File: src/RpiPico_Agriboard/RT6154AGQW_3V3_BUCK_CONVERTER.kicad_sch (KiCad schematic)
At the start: 14 parts, among them U1 RT6154A/B

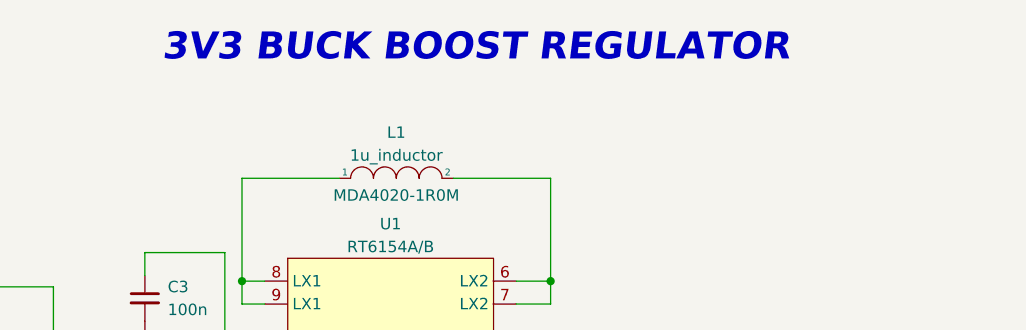
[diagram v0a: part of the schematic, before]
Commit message: Revert "schematic updates completed"
This reverts commit 0124993096667d53f20fd59dec80d3f5a1efcd43.
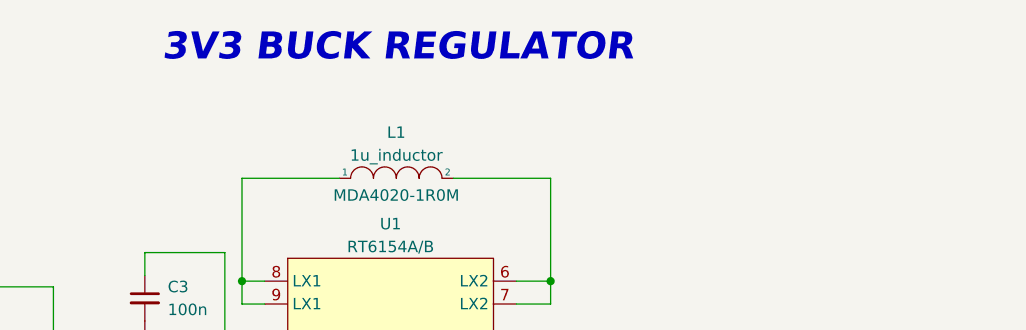
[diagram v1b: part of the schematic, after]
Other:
- note added: "3V3 BUCK REGULATOR"
- note removed: "3V3 BUCK BOOST REGULATOR"
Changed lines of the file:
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@@
     (stroke (width 0) (type default))
   )
-  (text "3V3 BUCK BOOST REGULATOR" (at 137.16 50.8 0)
+  (text "3V3 BUCK REGULATOR" (at 137.16 50.8 0)
     (effects (font (size 3 3) bold italic) (justify left bottom))
   )

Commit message: schematic updates completed
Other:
- note added: "3V3 BUCK BOOST REGULATOR"
- note removed: "3V3 BUCK REGULATOR"
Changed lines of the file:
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@@
     (stroke (width 0) (type default))
   )
-  (text "3V3 BUCK REGULATOR" (at 137.16 50.8 0)
+  (text "3V3 BUCK BOOST REGULATOR" (at 137.16 50.8 0)
     (effects (font (size 3 3) bold italic) (justify left bottom))
   )
